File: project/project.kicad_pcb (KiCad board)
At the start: 2 copper layers, 45 x 60 mm, 35 parts, among them J1 ssd1306 oled, SW1 USR_BTN, T1 xh3p, T2 xh3p, T3 xh3p, T4 xh3p, T5 xh3p, T6 xh3p, T7 xh3p, T8 xh3p, U1 esp32-c3-supermini

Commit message: everything has changed
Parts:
- removed the R15 at (114.5, 108.5)
- removed the R16 at (114.5, 104.4)
- removed kibuzzard-6696783F: G***, kibuzzard-6696783F
- added C1: 10u, Capacitor_SMD:C_0805_2012Metric_Pad1.18x1.45mm_HandSolder, F.Cu at (144.8, 79.5)
- added D2: LED, LED_SMD:LED_0805_2012Metric_Pad1.15x1.40mm_HandSolder, F.Cu at (162.3, 112.0)
- added R18: 330, Resistor_SMD:R_0805_2012Metric, F.Cu at (160.3, 112.0)
- added R19: 4k7, Resistor_SMD:R_0805_2012Metric, F.Cu at (149.8, 79.5)
- added R2: 4k7, Resistor_SMD:R_0805_2012Metric, F.Cu at (139.8, 73.0)
- added R20: 4k7, Resistor_SMD:R_0805_2012Metric, F.Cu at (147.3, 79.5)
- added R21: 330, Resistor_SMD:R_0805_2012Metric, F.Cu at (130.3, 112.0)
- added R22: 330, Resistor_SMD:R_0805_2012Metric, F.Cu at (164.3, 112.0)
- added R3: 330, Resistor_SMD:R_0805_2012Metric, F.Cu at (139.8, 79.5)
- added SW1: USR_BTN, Button_Switch_SMD:SW_SPST_PTS645, F.Cu at (132.3, 120.0)
- added kibuzzard-66DA8205: G***, kibuzzard-66DA8205, F.Cu at (146.3, 92.0)
- added kibuzzard-66DA82B0: G***, kibuzzard-66DA82B0, B.Cu at (131.3, 122.0)
- added kibuzzard-66DA8492: G***, kibuzzard-66DA8492, B.Cu at (139.3, 89.0)
- J1: footprint -local:oled_i2c_128x32_ssd1306 -> -local:oled_i2c_128x64_ssd1306
- T1, T2, T3, T4, T5, T6, T7, T8: value xh3p -> PJ-242; footprint -local:JST_XH_S3B-XH-SM4-TB_1x03-1MP_P2.50mm_Horizontal -> -local:PJ-242
- kibuzzard-669677F3: moved to B.Cu
- moved R9 99.9 mm to (154.8, 73.0)
- moved R10 89.5 mm to (154.8, 69.5), turned to -90 degrees
- moved T5 85.8 mm to (167.3, 72.0)
- moved U1 71.3 mm to (155.5, 130.0), turned to 180 degrees
- moved J1 70.9 mm to (147.3, 72.0), turned to 90 degrees
- moved R11 68.5 mm to (154.8, 83.0), turned to 90 degrees
- moved R12 68.1 mm to (154.8, 79.5), turned to -90 degrees
- moved R1 67.0 mm to (139.8, 69.5)
- moved T6 66.3 mm to (167.3, 82.0)
- moved kibuzzard-669677F3 65.2 mm to (154.8, 87.0), turned to 90 degrees
- moved R16 64.5 mm to (154.8, 99.5)
- moved G1 64.4 mm to (162.3, 128.0)
- moved R15 64.3 mm to (154.8, 103.0)
- moved SW2 63.2 mm to (162.3, 120.0), turned to -90 degrees
- moved H1 63.1 mm to (147.3, 103.0), turned to 180 degrees
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- renumbered C1 to C2, R3 to R15, R2 to R16, SW1 to SW2
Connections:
- R1 pad 1: LED -> Net-(R1-Pad1)
- R1 pad 2: Net-(D1-Pad1) -> +3V3
- R10 pad 1: +3V3 -> T5
- R10 pad 2: T5 -> +3V3
- R11 pad 1: +3V3 -> Net-(R11-Pad1)
- R11 pad 2: Net-(R11-Pad2) -> +3V3
- R12 pad 1: +3V3 -> T6
- R12 pad 2: T6 -> +3V3
- R13 pad 1: +3V3 -> Net-(R13-Pad1)
- R13 pad 2: Net-(R13-Pad2) -> +3V3
- R14 pad 1: +3V3 -> T7
- R14 pad 2: T7 -> +3V3
- R15 pad 1: +3V3 -> Net-(R15-Pad1)
- R15 pad 2: Net-(R3-Pad2) -> +3V3
- R16 pad 1: +3V3 -> T8
- R16 pad 2: T1 -> +3V3
- R17 pad 1: +3V3 -> Net-(D1-Pad1)
- R17 pad 2: Net-(R17-Pad2) -> LED
- R4 pad 1: +3V3 -> T2
- R4 pad 2: T2 -> +3V3
- R5 pad 1: +3V3 -> Net-(R5-Pad1)
- R5 pad 2: Net-(R5-Pad2) -> +3V3
- R6 pad 1: +3V3 -> T3
- R6 pad 2: T3 -> +3V3
- R7 pad 1: +3V3 -> Net-(R7-Pad1)
- R7 pad 2: Net-(R7-Pad2) -> +3V3
- R8 pad 1: +3V3 -> T4
- R8 pad 2: T4 -> +3V3
- R9 pad 1: +3V3 -> Net-(R9-Pad1)
- R9 pad 2: Net-(R9-Pad2) -> +3V3
- SW2 pad 1: BTN -> Net-(R22-Pad2)
- U1 pad 1: T1 -> T5
- U1 pad 10: T6 -> T3
- U1 pad 11: BTN -> BTN1
- U1 pad 12: T5 -> T2
- U1 pad 13: T8 -> T1
- U1 pad 2: T3 -> T6
- U1 pad 3: T4 -> T7
- U1 pad 6: T2 -> T8
- U1 pad 8: unconnected-(U1-Pad8) -> BTN2
- U1 pad 9: T7 -> T4
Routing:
- net +3V3: track 231.6 -> 166.3 mm, vias 19 -> 2
- net T1: track 9.23 -> 64.6 mm, vias 3 -> 0
- net T7: track 10.2 -> 58.8 mm
- net T2: track 8.04 -> 50.2 mm
- net BTN: track 42.0 -> 0.00 mm, vias 2 -> 0
- net T6: track 29.3 -> 70.3 mm, vias 2 -> 0
- net T5: track 48.8 -> 84.2 mm, vias 2 -> 0
- net SCL: track 32.0 -> 58.5 mm, vias 2 -> 0
- net T4: track 45.1 -> 18.8 mm, vias 2 -> 0
- net SDA: track 32.9 -> 57.9 mm, vias 2 -> 0
- net LED: track 9.52 -> 31.4 mm, vias 0 -> 4
- net T8: track 7.35 -> 28.3 mm, vias 0 -> 2
- net Net-(R5-Pad1): track 0.00 -> 13.0 mm, vias 0 -> 2
- net Net-(R7-Pad1): track 0.00 -> 13.0 mm, vias 0 -> 2
- net Net-(R15-Pad1): track 0.00 -> 12.5 mm, vias 0 -> 2
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- removed copper zone on B.Cu, net +3V3
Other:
- board size 45 x 60 mm -> 40 x 65 mm
- board text added: "GND|3V3|SCL|SDA"
- board text added: "Tip - DATA Ring1 - NC Ring2 - GND Sleeve - VCC"

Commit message: adding link and qr code
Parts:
- removed kibuzzard-66DA82B0: G***, kibuzzard-66DA82B0
- removed kibuzzard-66DA8492: G***, kibuzzard-66DA8492
- added G***: LOGO, -local:qr, B.Cu at (151.8, 123.0)
- added kibuzzard-66E2F5A0: G***, kibuzzard-66E2F5A0, B.Cu at (131.3, 122.0)
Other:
- board text added: "http://temp-1w8-pro.makerspace.lt/v1.1"

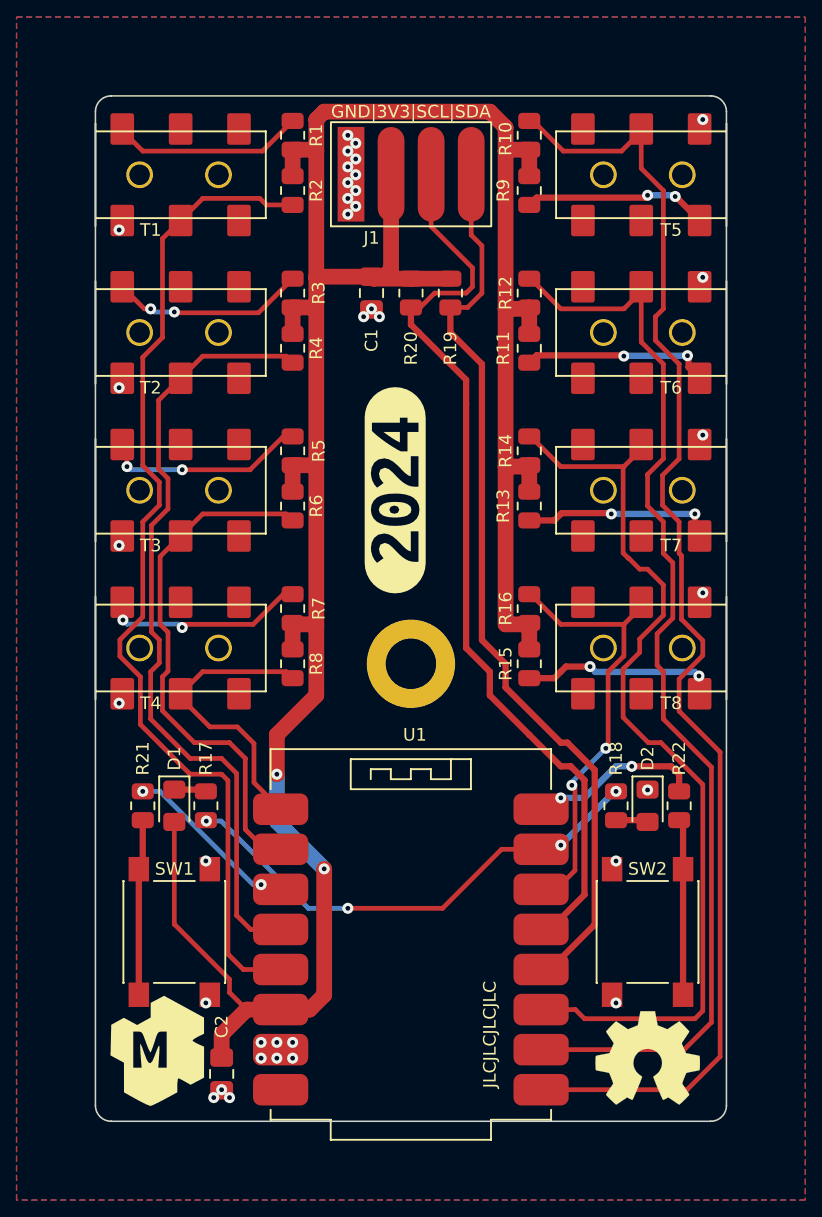
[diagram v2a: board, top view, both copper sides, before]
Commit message: fixed bugs from v1.0
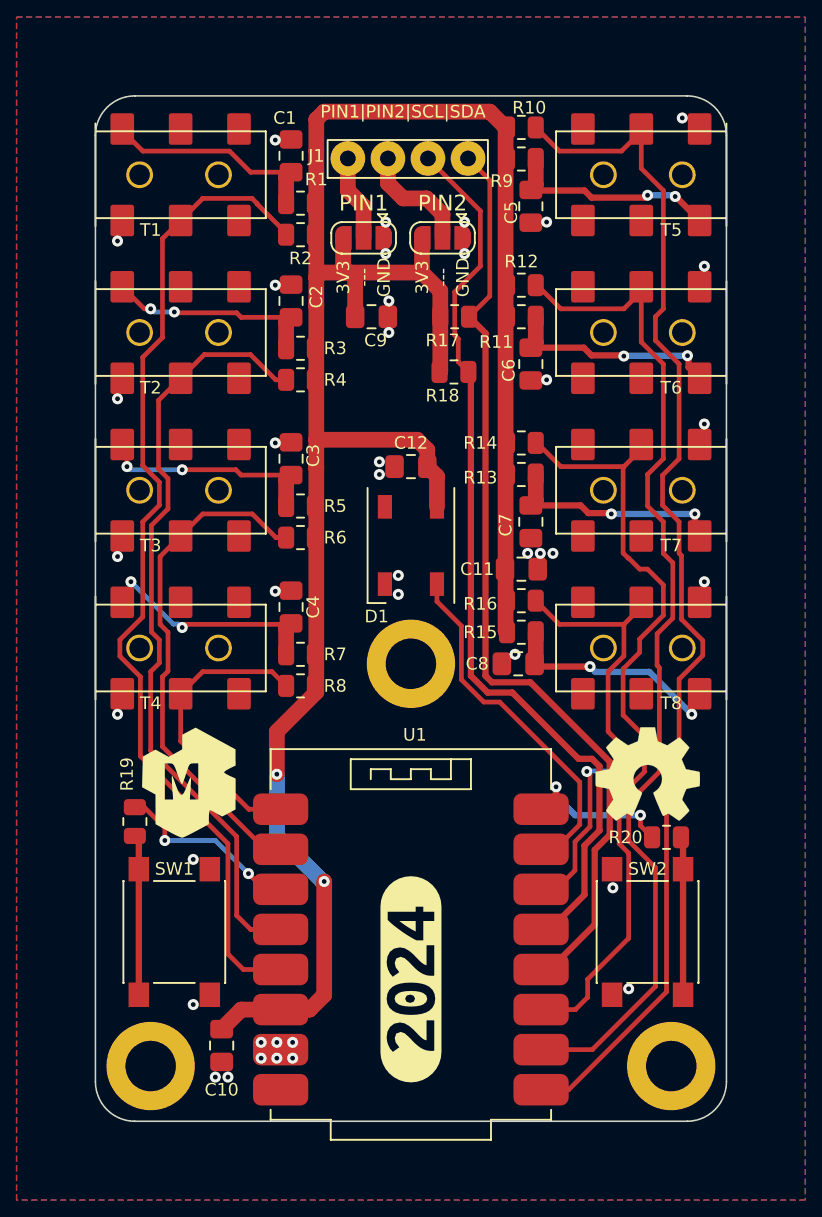
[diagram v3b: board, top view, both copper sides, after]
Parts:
- removed D2: LED, LED_SMD:LED_0805_2012Metric_Pad1.15x1.40mm_HandSolder
- removed the R17 at (134.3, 112.0)
- removed the R18 at (160.3, 112.0)
- removed kibuzzard-66E2F5A0: G***, kibuzzard-66E2F5A0
- added C11: 10u, Capacitor_SMD:C_0805_2012Metric_Pad1.18x1.45mm_HandSolder, F.Cu at (154.3, 97.0)
- added C12: 100n, Capacitor_SMD:C_0805_2012Metric_Pad1.18x1.45mm_HandSolder, F.Cu at (147.3, 90.5)
- added C2: 100n, Capacitor_SMD:C_0805_2012Metric_Pad1.18x1.45mm_HandSolder, F.Cu at (139.7, 80.0)
- added C3: 100n, Capacitor_SMD:C_0805_2012Metric_Pad1.18x1.45mm_HandSolder, F.Cu at (139.7, 90.0)
- added C4: 100n, Capacitor_SMD:C_0805_2012Metric_Pad1.18x1.45mm_HandSolder, F.Cu at (139.7, 99.4)
- added C5: 100n, Capacitor_SMD:C_0805_2012Metric_Pad1.18x1.45mm_HandSolder, F.Cu at (154.9, 74.0)
- added C6: 100n, Capacitor_SMD:C_0805_2012Metric_Pad1.18x1.45mm_HandSolder, F.Cu at (154.9, 84.0)
- added C7: 100n, Capacitor_SMD:C_0805_2012Metric_Pad1.18x1.45mm_HandSolder, F.Cu at (154.9, 94.0)
- added C8: 100n, Capacitor_SMD:C_0805_2012Metric_Pad1.18x1.45mm_HandSolder, F.Cu at (154.1, 103.0)
- added C9: 10u, Capacitor_SMD:C_0805_2012Metric_Pad1.18x1.45mm_HandSolder, F.Cu at (144.8, 81.0)
- added H1: MP, MountingHole:MountingHole_3.2mm_M3_DIN965_Pad, F.Cu at (130.8, 128.5)
- added H3: MP, MountingHole:MountingHole_3.2mm_M3_DIN965_Pad, F.Cu at (163.8, 128.5)
- added JP1: PIN2, Jumper:SolderJumper-3_P1.3mm_Open_RoundedPad1.0x1.5mm, F.Cu at (149.3, 76.0)
- added JP2: PIN1, Jumper:SolderJumper-3_P1.3mm_Open_RoundedPad1.0x1.5mm, F.Cu at (144.3, 76.0)
- added kibuzzard-67074305: G***, kibuzzard-67074305, B.Cu at (164.5, 114.0)
- C1: value 10u -> 100n
- D1: value LED -> WS2812B; footprint LED_SMD:LED_0805_2012Metric_Pad1.15x1.40mm_HandSolder -> LED_SMD:LED_WS2812B_PLCC4_5.0x5.0mm_P3.2mm
- J1: footprint -local:oled_i2c_128x64_ssd1306 -> -local:oled_i2c_1.3_128x64_ssd1306
- moved kibuzzard-66DA8205 31.0 mm to (147.3, 123.0)
- moved D1 22.3 mm to (147.3, 95.5)
- moved G1 18.0 mm to (162.3, 110.0)
- moved G2 17.1 mm to (132.8, 110.5)
- moved kibuzzard-669677F3 14.1 mm to (140.8, 89.0)
- moved C1 10.1 mm to (139.7, 70.8), turned to 90 degrees
- moved R18 5.70 mm to (150.0, 84.5), turned to 180 degrees
- moved R1 4.33 mm to (140.3, 73.8), turned to 0 degrees
- moved R3 3.54 mm to (140.3, 83.0), turned to 0 degrees
- moved R5 3.54 mm to (140.3, 93.0), turned to 0 degrees
- moved R7 2.94 mm to (140.3, 102.4), turned to 0 degrees
- moved R2 2.84 mm to (140.3, 75.8), turned to 0 degrees
- moved R20 2.15 mm to (163.5, 114.0), turned to 0 degrees
- moved R11 2.06 mm to (154.3, 81.0), turned to 180 degrees
- moved R13 2.06 mm to (154.3, 91.0), turned to 180 degrees
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- renumbered C2 to C10, H1 to H2, R19 to R17, R20 to R18, R21 to R19, R22 to R20
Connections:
- C1 pad 1: +3V3 -> Net-(R1-Pad1)
- D1 pad 1: Net-(D1-Pad1) -> +3V3
- D1 pad 2: +3V3 -> unconnected-(D1-Pad2)
- J1 pad 1: GND -> Net-(J1-Pad1)
- J1 pad 2: +3V3 -> Net-(JP1-Pad2)
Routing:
- net +3V3: track 166.3 -> 142.3 mm
- net T7: track 58.8 -> 50.0 mm
- net LED: track 31.4 -> 22.7 mm, vias 4 -> 0
- net Net-(JP1-Pad2): track 0.00 -> 7.34 mm
- net T5: track 84.2 -> 77.0 mm
- net Net-(J1-Pad1): track 0.00 -> 5.45 mm
- net T6: track 70.3 -> 65.0 mm
- net Net-(R15-Pad1): track 12.5 -> 14.8 mm
- net Net-(R7-Pad1): track 13.0 -> 15.1 mm
- net Net-(D2-Pad2): track 2.05 -> 0.00 mm
- net Net-(D1-Pad1): track 2.05 -> 0.00 mm
- net Net-(R13-Pad1): track 12.2 -> 14.2 mm
- net Net-(R9-Pad1): track 11.7 -> 13.7 mm
- net Net-(R11-Pad1): track 12.0 -> 14.0 mm
- net SDA: track 57.9 -> 59.8 mm
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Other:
- outline, holes or cut-outs redrawn
- board text added: "3V3 --- GND"
- board text added: "PIN1|PIN2|SCL|SDA"
- board text added: "http://temp-1w8-pro.makerspace.lt/v2.0"
- board text removed: "GND|3V3|SCL|SDA"
- board text removed: "JLCJLCJLCJLC"
- board text removed: "http://temp-1w8-pro.makerspace.lt/v1.1"

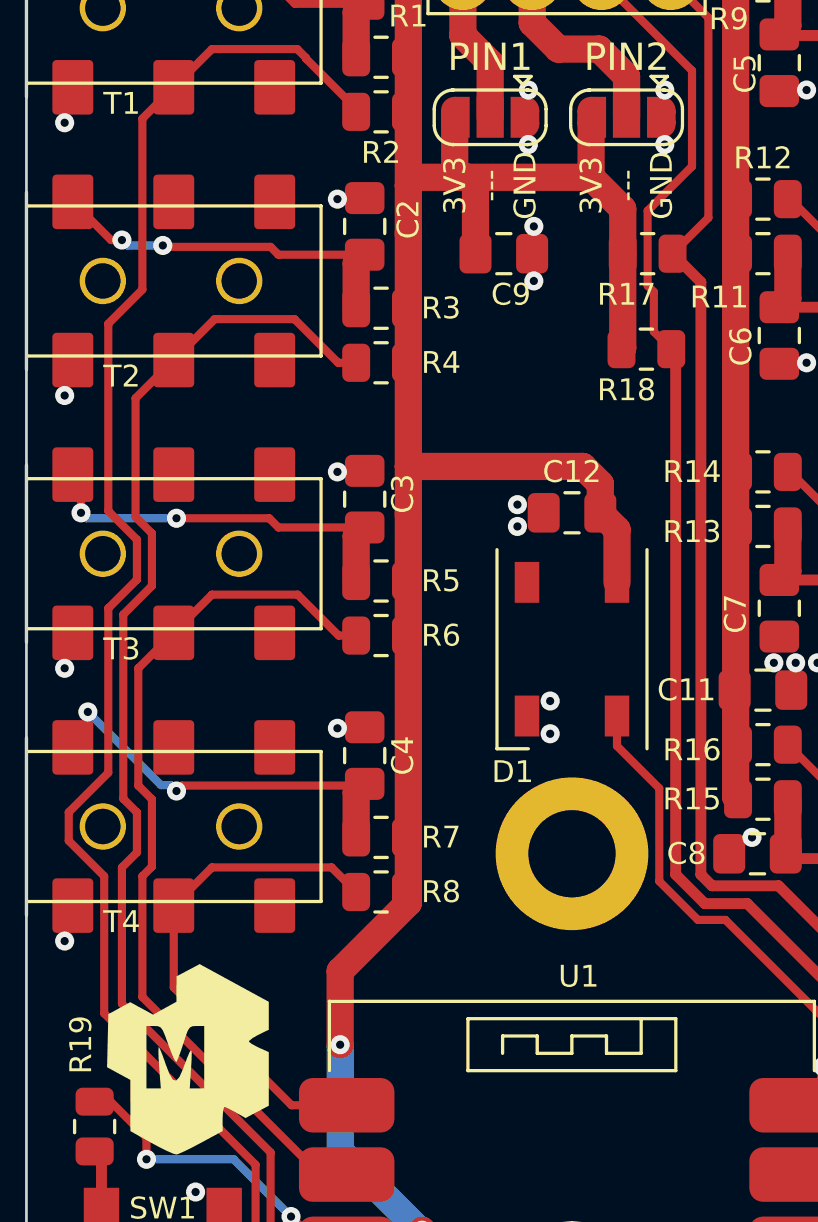
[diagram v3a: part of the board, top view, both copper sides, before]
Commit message: adding hard reset for sensors, removing rgb led
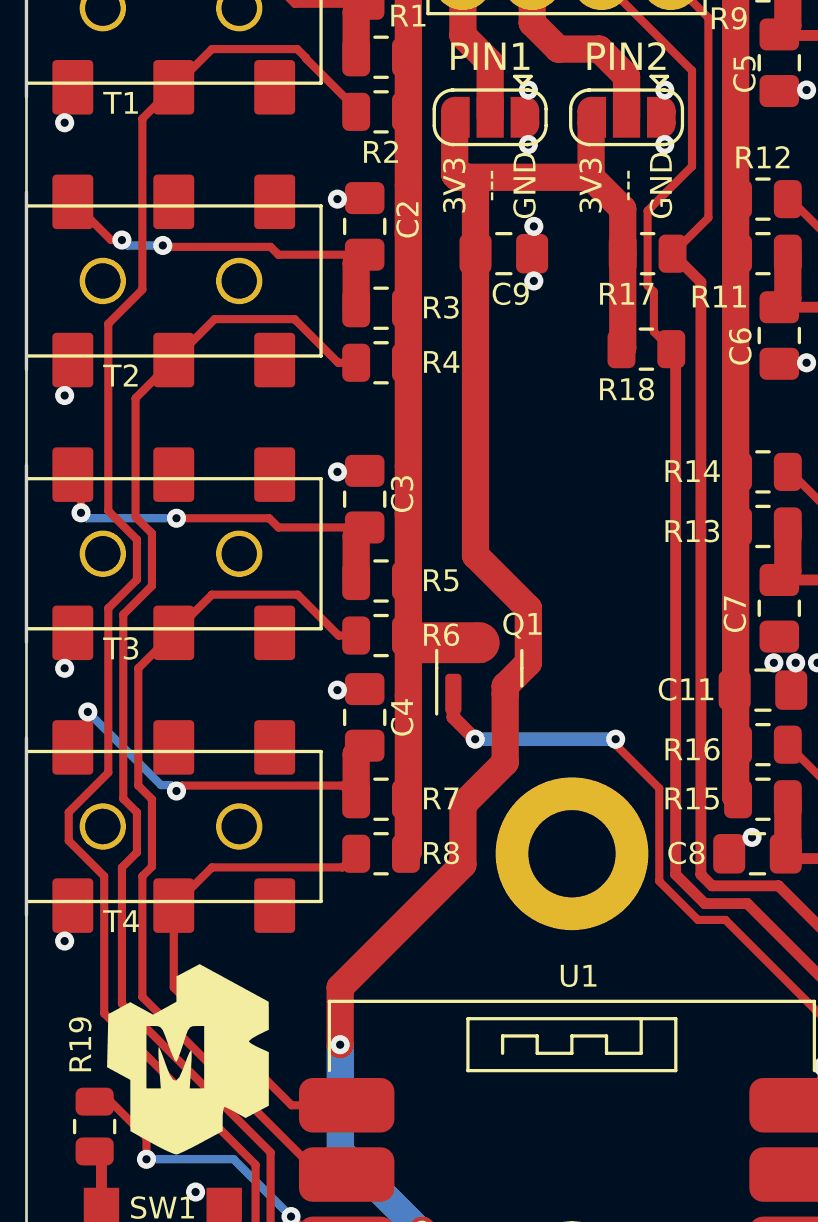
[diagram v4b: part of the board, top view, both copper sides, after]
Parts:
- removed C12: 100n, Capacitor_SMD:C_0805_2012Metric_Pad1.18x1.45mm_HandSolder
- removed D1: WS2812B, LED_SMD:LED_WS2812B_PLCC4_5.0x5.0mm_P3.2mm
- removed kibuzzard-67074305: G***, kibuzzard-67074305
- added Q1: AO3401A, Package_TO_SOT_SMD:SOT-23, F.Cu at (143.9, 96.2)
- added kibuzzard-674CCC3B: G***, kibuzzard-674CCC3B, B.Cu at (164.5, 114.0)
- moved C4 1.40 mm to (139.7, 98.0)
- moved R7 1.40 mm to (140.3, 101.0)
- moved R8 1.40 mm to (140.3, 103.0)
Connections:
- C11 pad 1: +3V3 -> /_TVCC
- R1 pad 2: +3V3 -> /_TVCC
- R10 pad 2: +3V3 -> /_TVCC
- R11 pad 2: +3V3 -> /_TVCC
- R12 pad 2: +3V3 -> /_TVCC
- R13 pad 2: +3V3 -> /_TVCC
- R14 pad 2: +3V3 -> /_TVCC
- R15 pad 2: +3V3 -> /_TVCC
- R16 pad 2: +3V3 -> /_TVCC
- R2 pad 2: +3V3 -> /_TVCC
- R3 pad 2: +3V3 -> /_TVCC
- R4 pad 2: +3V3 -> /_TVCC
- R5 pad 2: +3V3 -> /_TVCC
- R6 pad 2: +3V3 -> /_TVCC
- R7 pad 2: +3V3 -> /_TVCC
- R8 pad 2: +3V3 -> /_TVCC
- R9 pad 2: +3V3 -> /_TVCC
- U1 pad 7: LED -> 1W_NRST
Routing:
- net /_TVCC: track 0.00 -> 82.2 mm
- net +3V3: track 142.3 -> 74.4 mm
- net 1W_NRST: track 0.00 -> 29.0 mm, vias 0 -> 2
- net LED: track 22.7 -> 0.00 mm
- net GND: vias 40 -> 36
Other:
- board text added: "http://temp-1w8-pro.makerspace.lt/v3.0"
- board text removed: "http://temp-1w8-pro.makerspace.lt/v2.0"
